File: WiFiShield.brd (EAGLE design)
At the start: 68.6 x 53.3 mm, 37 parts, among them IC1 MC74VHCT50A, IC2 74AHC1G125, IC4 SPX3819M5-L-3-3, IC5 CC3000MOD, J10 Test, J2 Mode, J8 ARDUINO-SHIELD_R3, J9 U.FL-R-SMT-1(10)

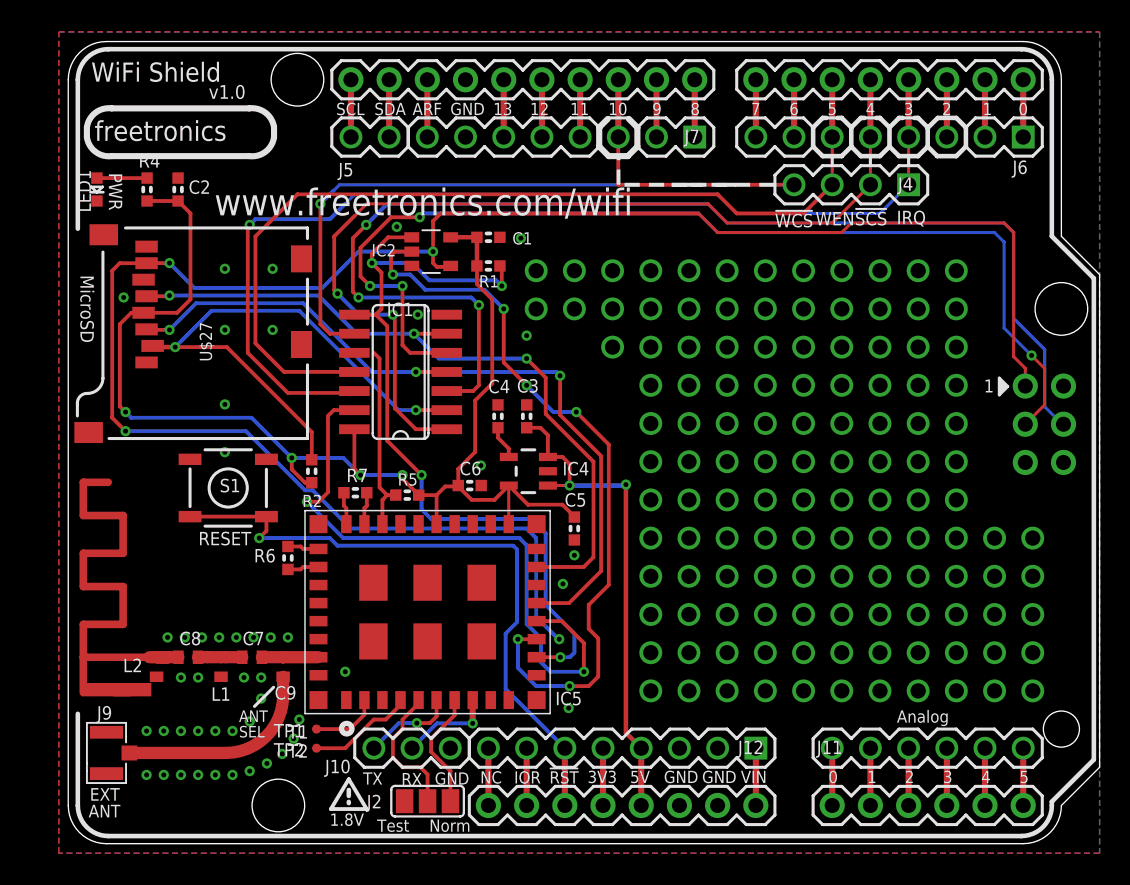
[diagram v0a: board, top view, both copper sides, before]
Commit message: Switch to chip antenna, final pre-prototype design review
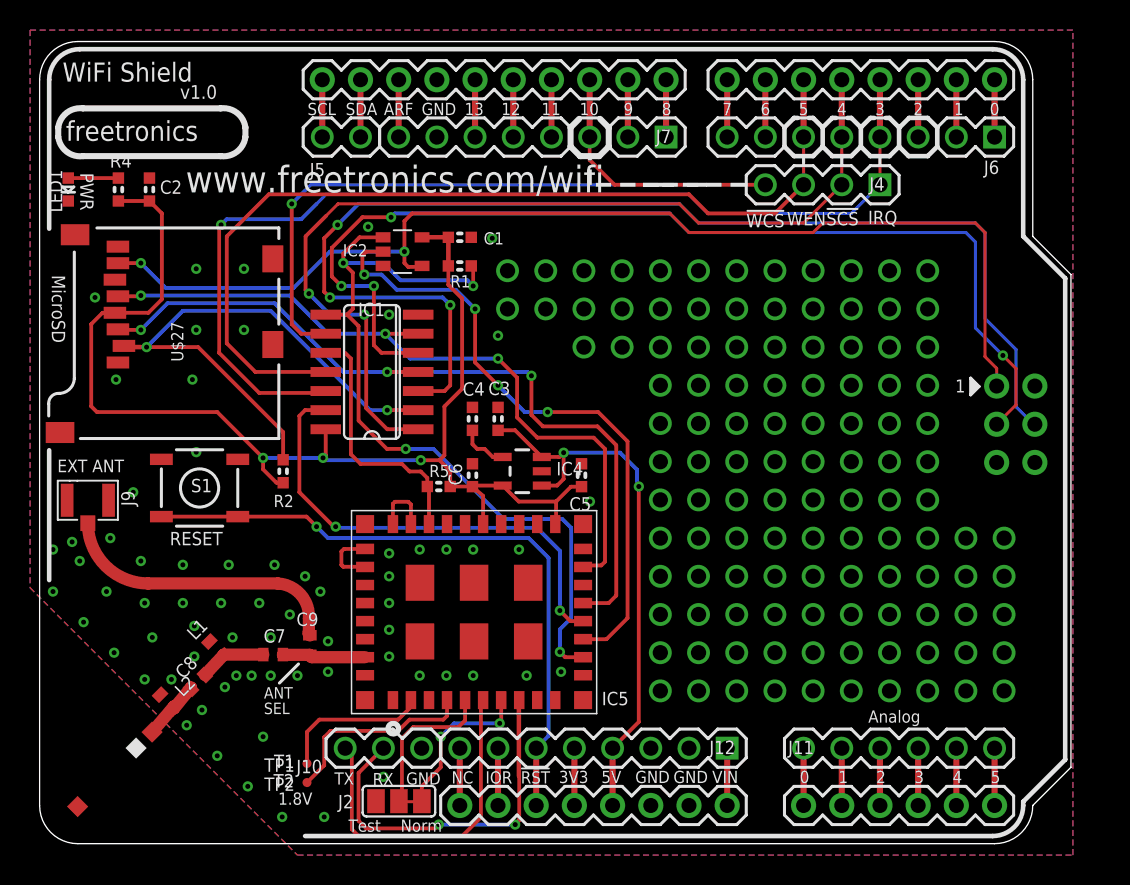
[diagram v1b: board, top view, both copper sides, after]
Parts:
- removed R6, R7: 0R, freetronics-master-v1:0603
- ANT1: value ANTENNA -> 2500AT44M0400; device adafruit:RN-ANT -> freetronics-angus:2500AT44M0400
- J8: device freetronics-angus:ARDUINO-SHIELD_R3 -> freetronics-angus:ARDUINO-SHIELD_R3_NOHOLES
- moved J9 16.9 mm to (3.21, 22.8), turned to 90 degrees
- moved ANT1 5.77 mm to (5.00, 4.94), turned to 225 degrees
- moved C5 3.58 mm to (36.0, 24.5), turned to 90 degrees
- moved IC5 3.09 mm to (28.9, 15.4)
- moved L2 2.40 mm to (8.47, 9.45), turned to 135 degrees
- moved TP1 2.37 mm to (17.8, 5.33)
- moved TP2 2.37 mm to (17.8, 4.06)
- moved C9 2.30 mm to (18.0, 13.2), turned to 270 degrees
- moved R5 2.17 mm to (26.5, 23.8)
- moved C3 1.91 mm to (30.5, 28.2)
- moved IC1 1.91 mm to (22.1, 31.4)
- moved IC2 1.91 mm to (24.1, 39.4)
- moved J10 1.91 mm to (20.3, 6.35)
- moved J11 1.91 mm to (50.8, 6.35)
- moved J12 1.91 mm to (45.7, 6.35)
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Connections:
- removed net N$15: IC5.30, R6.2
- removed net N$5: IC5.29, R6.1
- net GND: no longer ANT1.GND
- net N$1: now also IC5.28; no longer R7.2
- net N$104: now also ANT1.P$1; no longer ANT1.FEED
- net N$2: now also IC5.29, IC5.30; no longer IC5.28, R7.1
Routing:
- net MISO_TRISTATE: track 126.9 -> 76.3 mm, vias 4 -> 2
- net WL_UART_RX: track 6.26 -> 29.7 mm, vias 1 -> 2
- net WL_UART_TX: track 6.14 -> 22.7 mm, vias 1 -> 0
- net N$42: track 41.4 -> 31.7 mm
- net CC3000_MISO: track 49.4 -> 42.3 mm, vias 6 -> 4
- net N$28: track 7.09 -> 13.3 mm
- net N$30: track 13.1 -> 18.8 mm
- net N$29: track 4.55 -> 10.2 mm
- net +5V: track 33.1 -> 37.0 mm
- net CC3000_EN_3V3: track 12.5 -> 16.0 mm
- net WL_EN1: track 7.90 -> 10.7 mm, vias 0 -> 2
- net MOSI_3V3: track 51.6 -> 53.8 mm
- net N$5: track 2.10 -> 0.00 mm
- net N$15: track 2.10 -> 0.00 mm
- net N$2: track 2.15 -> 4.17 mm
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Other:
- board text added: "EXT ANT"
- board text removed: "EXT"

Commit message: Minor cleanup
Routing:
- net N$42: track 31.7 -> 32.5 mm
- net N$78: track 43.7 -> 44.3 mm
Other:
- board text added: "v0.1"
- board text removed: "v1.0"

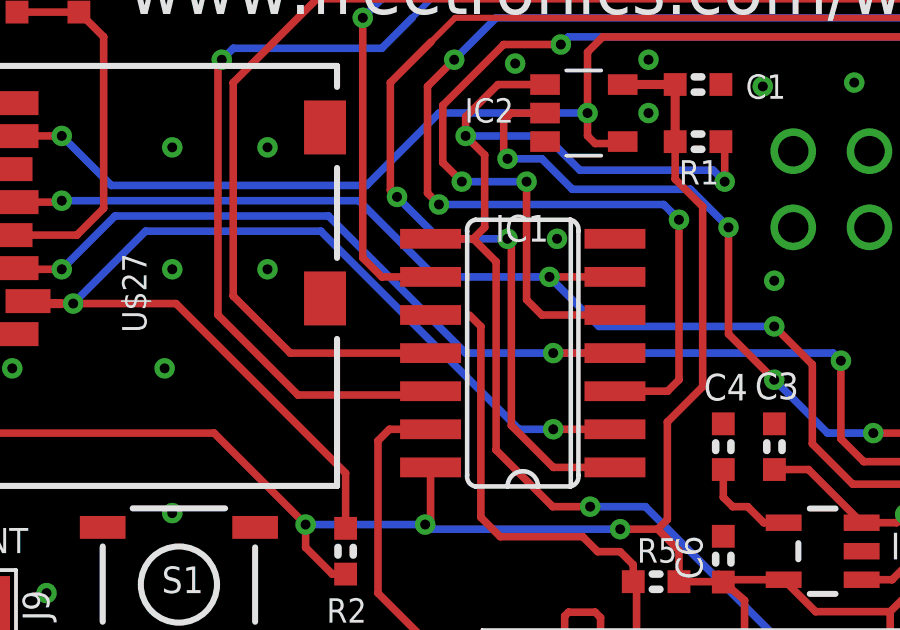
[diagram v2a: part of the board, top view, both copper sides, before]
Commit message: Replace accidentally deleted wire
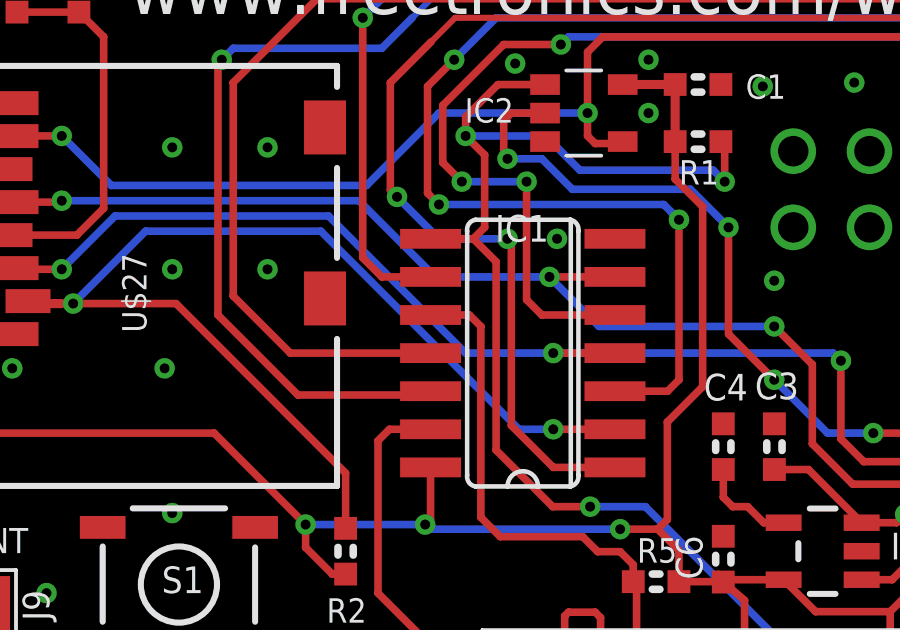
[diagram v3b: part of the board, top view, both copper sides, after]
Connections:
- removed net N$3: IC1.10
- net CC3000_EN_3V3: now also IC1.10
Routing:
- net CC3000_EN_3V3: track 16.0 -> 17.3 mm
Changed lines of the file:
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@@
 <wire x1="25.345" y1="24.75" x2="25.7805" y2="24.3145" width="0.254" layer="1"/>
 <wire x1="25.7805" y1="24.3145" x2="25.7805" y2="23.75" width="0.254" layer="1"/>
+<contactref element="IC1" pad="10"/>
+<wire x1="20.32" y1="32.639" x2="19.0246" y2="32.639" width="0.254" layer="1"/>
 </signal>
 <signal name="MOSI_5V">
@@
 <wire x1="39.095" y1="15" x2="39.095" y2="26.75" width="0.254" layer="1"/>
 </signal>
-<signal name="N$3">
-<contactref element="IC1" pad="10"/>
-</signal>
 <signal name="N$7">

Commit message: Juggle antenna routing a bit
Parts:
- moved J9 9.21 mm to (10.6, 17.3), turned to 180 degrees
- moved L2 0.81 mm to (7.84, 8.94)
- moved ANT1 0.76 mm to (4.35, 4.54)
- moved C8 0.72 mm to (10.0, 10.2)
- moved L1 0.72 mm to (11.2, 12.5)
- moved C7 0.40 mm to (15.1, 12.4)
- moved C9 0.13 mm to (18.0, 13.1)
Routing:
- net N$30: track 18.8 -> 8.18 mm
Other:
- board text added: "v1.0"
- board text removed: "v0.1"

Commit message: Swap R1 to be pulldown on enable
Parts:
- moved R1 13.9 mm to (15.9, 45.5), turned to 90 degrees
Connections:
- net !CC3000_CS_3V3: no longer R1.2
- net +3V3: no longer R1.1
- net CC3000_EN_5V: now also R1.1
- net GND: now also R1.2
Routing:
- net !CC3000_CS_3V3: track 54.4 -> 43.7 mm, vias 4 -> 2
- net +3V3: track 82.8 -> 84.6 mm
- net CC3000_EN_5V: track 58.3 -> 60.1 mm
- net CC3000_IRQ_5V: track 65.8 -> 65.0 mm
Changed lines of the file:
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@@
 <setting verticaltext="up"/>
 </settings>
-<grid distance="10" unitdist="mil" unit="mil" style="lines" multiple="1" display="yes" altdistance="3.125" altunitdist="mil" altunit="mil"/>
+<grid distance="5" unitdist="mil" unit="mil" style="lines" multiple="1" display="yes" altdistance="3.125" altunitdist="mil" altunit="mil"/>
 <layers>
 <layer number="1" name="Top" color="4" fill="1" visible="yes" active="yes"/>
@@
 <wire x1="1.23825" y1="47.625" x2="2.88925" y2="48.895" width="0.4064" layer="21" curve="-90"/>
 <text x="1.524" y="50.673" size="1.27" layer="21" font="vector" ratio="17">WiFi Shield</text>
-<text x="8.9535" y="42.672" size="1.778" layer="21" font="vector" ratio="17">www.freetronics.com/wifi</text>
+<text x="8.5725" y="42.545" size="1.778" layer="21" font="vector" ratio="17">www.freetronics.com/wifi</text>
 <text x="22.86" y="43.4975" size="1.4732" layer="22" font="vector" ratio="17" rot="MR180">freetronics</text>
 <text x="1.74625" y="46.736" size="1.3208" layer="21" font="vector" ratio="17">freetronics</text>
@@
 <attribute name="VALUE" x="25.59" y="24.385" size="0.8128" layer="27" font="vector" ratio="15"/>
 </element>
-<element name="R1" library="freetronics-master-v1" package="0603" value="10k" x="27.94" y="38.4175" smashed="yes">
-<attribute name="PACKAGE" value="0603" x="27.94" y="38.4175" size="0.8128" layer="27" ratio="15" display="off"/>
-<attribute name="NAME" x="27.305" y="36.98875" size="0.8128" layer="25" font="vector" ratio="15"/>
-<attribute name="VALUE" x="26.82875" y="36.98875" size="0.8128" layer="27" font="vector" ratio="15"/>
+<element name="R1" library="freetronics-master-v1" package="0603" value="10k" x="15.9385" y="45.466" smashed="yes" rot="R90">
+<attribute name="PACKAGE" value="0603" x="15.9385" y="45.466" size="0.8128" layer="27" ratio="15" rot="R90" display="off"/>
+<attribute name="NAME" x="17.36725" y="44.831" size="0.8128" layer="25" font="vector" ratio="15" rot="R90"/>
+<attribute name="VALUE" x="17.36725" y="44.35475" size="0.8128" layer="27" font="vector" ratio="15" rot="R90"/>
 </element>
 <element name="R2" library="freetronics-master-v1" package="0603" value="10k" x="16.1925" y="24.765" smashed="yes" rot="R90">
@@
 <via x="8.763" y="18.796" extent="1-16" drill="0.3302"/>
 <via x="12.573" y="18.796" extent="1-16" drill="0.3302"/>
+<contactref element="R1" pad="2"/>
 </signal>
 <signal name="3V3">
@@
 <wire x1="5.23875" y1="42.7355" x2="7.3025" y2="42.7355" width="0.254" layer="1"/>
 <contactref element="R5" pad="1"/>
-<contactref element="R1" pad="1"/>
 <contactref element="R2" pad="1"/>
 <contactref element="C1" pad="2"/>
@@
 <wire x1="27.178" y1="40.3225" x2="25.4325" y2="40.3225" width="0.3048" layer="1"/>
 <wire x1="25.4325" y1="40.3225" x2="25.43" y2="40.32" width="0.2032" layer="1"/>
-<wire x1="27.178" y1="40.3225" x2="27.178" y2="38.4175" width="0.3048" layer="1"/>
 <contactref element="U$27" pad="4"/>
 <wire x1="16.1925" y1="24.003" x2="15.748" y2="24.003" width="0.254" layer="1"/>
@@
 <wire x1="30.7942" y1="23.815" x2="31.8592" y2="22.75" width="0.254" layer="1"/>
 <wire x1="31.8592" y1="22.75" x2="34.345" y2="22.75" width="0.254" layer="1"/>
-<wire x1="27.178" y1="38.4175" x2="27.178" y2="37.167" width="0.254" layer="1"/>
-<wire x1="27.178" y1="37.167" x2="28.095" y2="36.25" width="0.254" layer="1"/>
-<wire x1="28.095" y1="36.25" x2="28.095" y2="30.25" width="0.254" layer="1"/>
-<wire x1="28.095" y1="30.25" x2="26.9175" y2="29.0725" width="0.254" layer="1"/>
 <wire x1="25.345" y1="25.5" x2="26.595" y2="25.5" width="0.254" layer="1"/>
-<wire x1="26.595" y1="25.5" x2="26.9175" y2="25.8225" width="0.254" layer="1"/>
-<wire x1="26.9175" y1="25.8225" x2="26.9175" y2="29.0725" width="0.254" layer="1"/>
 <wire x1="27.3045" y1="23.75" x2="28.7705" y2="23.75" width="0.254" layer="1"/>
 <wire x1="28.7705" y1="23.75" x2="28.7825" y2="23.738" width="0.254" layer="1"/>
@@
 <wire x1="3.81" y1="28.702" x2="11.811" y2="28.702" width="0.254" layer="1"/>
 <wire x1="11.811" y1="28.702" x2="14.859" y2="25.654" width="0.254" layer="1"/>
+<wire x1="25.4325" y1="40.3225" x2="27.1145" y2="40.3225" width="0.254" layer="1"/>
+<wire x1="27.1145" y1="40.3225" x2="27.178" y2="40.386" width="0.254" layer="1"/>
+<wire x1="27.178" y1="40.386" x2="27.178" y2="39.497" width="0.254" layer="1"/>
+<wire x1="27.178" y1="39.497" x2="28.067" y2="38.608" width="0.254" layer="1"/>
+<wire x1="28.067" y1="38.608" x2="28.067" y2="29.972" width="0.254" layer="1"/>
+<wire x1="28.067" y1="29.972" x2="27.432" y2="29.337" width="0.254" layer="1"/>
+<wire x1="27.432" y1="29.337" x2="27.432" y2="26.337" width="0.254" layer="1"/>
+<wire x1="27.432" y1="26.337" x2="26.595" y2="25.5" width="0.254" layer="1"/>
 </signal>
 <signal name="WL_EN2">
@@
 <wire x1="27.845" y1="7.75" x2="24.845" y2="7.75" width="0.254" layer="1"/>
 <wire x1="24.845" y1="7.75" x2="24.095" y2="7" width="0.254" layer="1"/>
-<wire x1="24.095" y1="3.028875" x2="23.891875" y2="2.82575" width="0" layer="19" extent="1-1"/>
+<wire x1="23.891875" y1="2.82575" x2="24.095" y2="3.028875" width="0.254" layer="1"/>
 </signal>
 <signal name="WL_EN1">
@@
 <wire x1="18.8976" y1="29.972" x2="19.0246" y2="30.099" width="0.254" layer="1"/>
 <wire x1="18.415" y1="42.545" x2="17.399" y2="41.529" width="0.254" layer="16"/>
-<wire x1="17.399" y1="41.529" x2="12.446" y2="41.529" width="0.254" layer="16"/>
-<wire x1="12.446" y1="41.529" x2="12.065" y2="41.148" width="0.254" layer="16"/>
-<via x="12.065" y="41.148" extent="1-16" drill="0.3302"/>
-<wire x1="12.065" y1="41.148" x2="11.938" y2="41.021" width="0.254" layer="1"/>
-<wire x1="11.938" y1="41.021" x2="11.938" y2="32.639" width="0.254" layer="1"/>
 <wire x1="11.938" y1="32.639" x2="14.605" y2="29.972" width="0.254" layer="1"/>
+<wire x1="17.399" y1="41.529" x2="13.843" y2="41.529" width="0.254" layer="16"/>
+<via x="13.843" y="41.529" extent="1-16" drill="0.3302"/>
+<wire x1="13.843" y1="41.529" x2="11.938" y2="39.624" width="0.254" layer="1"/>
+<wire x1="11.938" y1="39.624" x2="11.938" y2="32.639" width="0.254" layer="1"/>
 </signal>
 <signal name="N$43">
@@
 <contactref element="IC5" pad="12"/>
 <contactref element="IC1" pad="8"/>
-<contactref element="R1" pad="2"/>
 <contactref element="IC2" pad="1"/>
 <wire x1="21.209" y1="28.136" x2="21.209" y2="34.417" width="0.254" layer="1"/>
@@
 <wire x1="20.447" y1="35.179" x2="20.828" y2="35.56" width="0.254" layer="1"/>
 <wire x1="21.27" y1="40.32" x2="22.84" y2="40.32" width="0.254" layer="1"/>
-<wire x1="24.003" y1="37.465" x2="28.448" y2="37.465" width="0.254" layer="16"/>
-<wire x1="28.448" y1="37.465" x2="28.829" y2="37.084" width="0.254" layer="16"/>
-<via x="28.829" y="37.084" extent="1-16" drill="0.3302"/>
-<wire x1="28.829" y1="37.084" x2="28.829" y2="38.2905" width="0.254" layer="1"/>
-<wire x1="28.829" y1="38.2905" x2="28.702" y2="38.4175" width="0.254" layer="1"/>
 <wire x1="21.27" y1="40.32" x2="20.193" y2="39.243" width="0.254" layer="1"/>
 <wire x1="20.193" y1="39.243" x2="20.193" y2="38.608" width="0.254" layer="1"/>
-<via x="20.193" y="38.608" extent="1-16" drill="0.3302"/>
 <wire x1="20.828" y1="35.56" x2="20.828" y2="37.973" width="0.254" layer="1"/>
 <wire x1="20.828" y1="37.973" x2="20.193" y2="38.608" width="0.254" layer="1"/>
-<wire x1="24.003" y1="37.465" x2="22.86" y2="38.608" width="0.254" layer="16"/>
-<wire x1="22.86" y1="38.608" x2="20.193" y2="38.608" width="0.254" layer="16"/>
 <wire x1="30.845" y1="21.59" x2="34.755" y2="21.59" width="0.254" layer="16"/>
 <wire x1="34.755" y1="21.59" x2="35.345" y2="21" width="0.254" layer="16"/>
@@
 <wire x1="19.0246" y1="31.369" x2="14.351" y2="31.369" width="0.254" layer="1"/>
 <wire x1="14.351" y1="31.369" x2="12.446" y2="33.274" width="0.254" layer="1"/>
-<wire x1="12.446" y1="33.274" x2="12.446" y2="40.386" width="0.254" layer="1"/>
 <wire x1="50.8" y1="43.815" x2="48.895" y2="41.91" width="0.254" layer="1"/>
 <wire x1="48.895" y1="41.91" x2="44.45" y2="41.91" width="0.254" layer="1"/>
-<wire x1="12.446" y1="40.386" x2="15.24" y2="43.18" width="0.254" layer="1"/>
-<wire x1="15.24" y1="43.18" x2="43.18" y2="43.18" width="0.254" layer="1"/>
+<wire x1="37.338" y1="43.18" x2="43.18" y2="43.18" width="0.254" layer="1"/>
 <wire x1="43.18" y1="43.18" x2="44.45" y2="41.91" width="0.254" layer="1"/>
+<contactref element="R1" pad="1"/>
+<wire x1="15.9385" y1="44.704" x2="35.814" y2="44.704" width="0.254" layer="1"/>
+<wire x1="35.814" y1="44.704" x2="37.338" y2="43.18" width="0.254" layer="1"/>
+<wire x1="12.446" y1="38.608" x2="12.446" y2="33.274" width="0.254" layer="1"/>
+<wire x1="15.9385" y1="44.704" x2="15.9385" y2="42.1005" width="0.254" layer="1"/>
+<wire x1="15.9385" y1="42.1005" x2="12.446" y2="38.608" width="0.254" layer="1"/>
 </signal>
 <signal name="CC3000_EN_3V3">

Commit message: Increase pad restring, move some traces around
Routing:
- net !CC3000_CS_3V3: track 43.7 -> 51.1 mm
- net N$42: track 32.5 -> 38.0 mm
- net N$78: track 44.3 -> 49.3 mm
- net WL_UART_RX: track 29.7 -> 25.1 mm
